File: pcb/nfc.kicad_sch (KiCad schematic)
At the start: 18 parts, among them U5 ST25R3916-AQWT, Y2 NX2016SA-27.12MHZ-STD-CZS-3

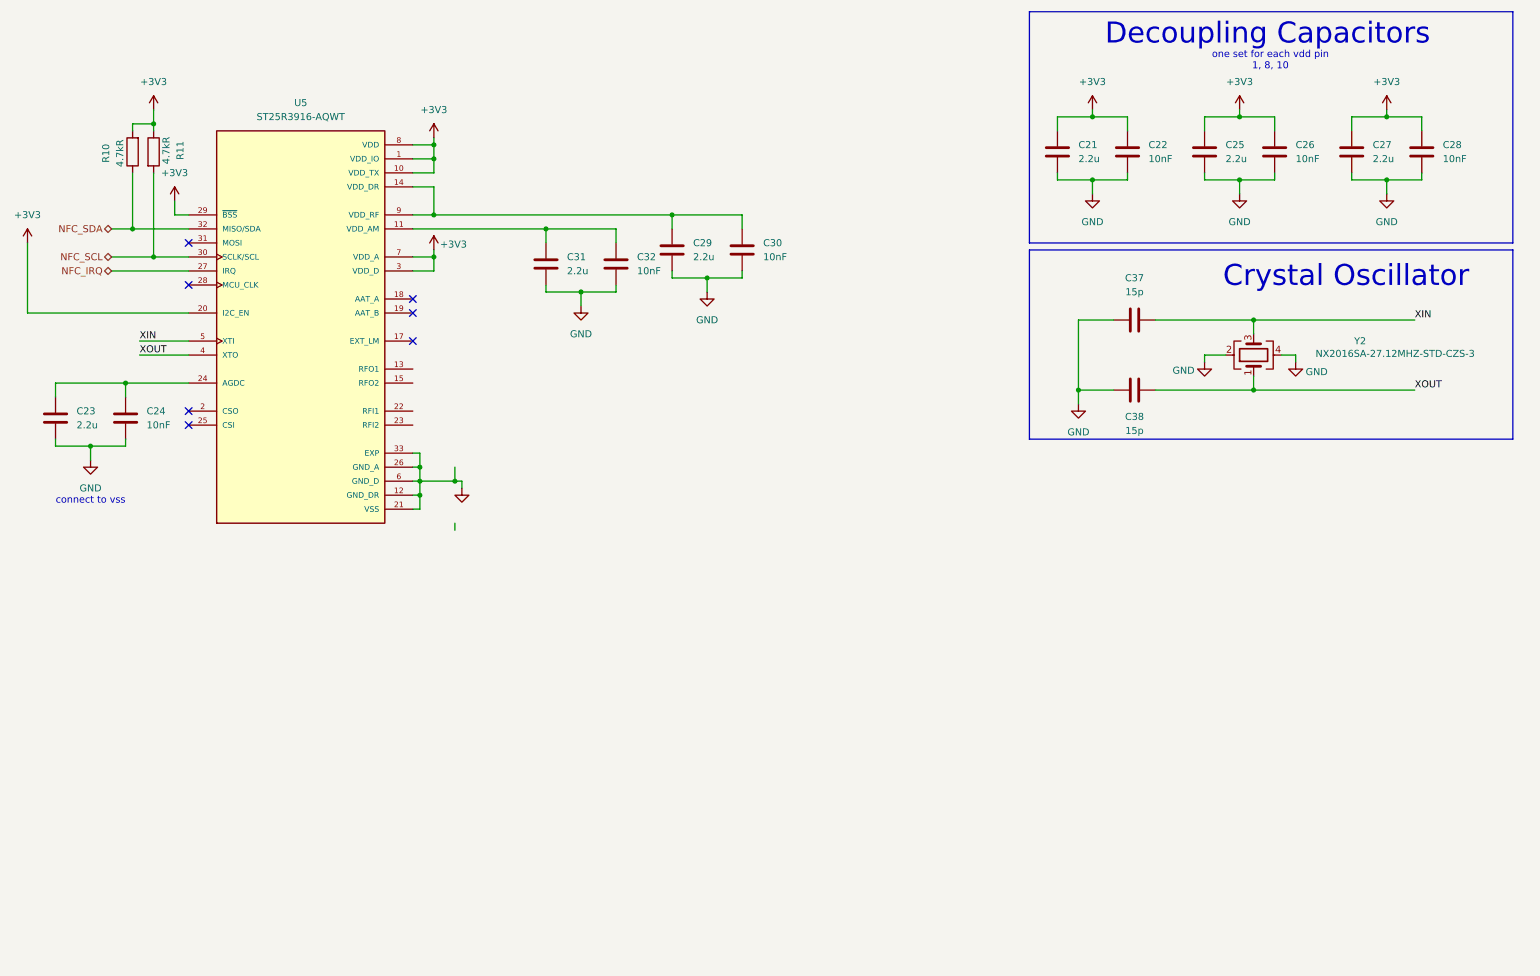
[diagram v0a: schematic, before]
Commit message: nfc tuning, new charger IC
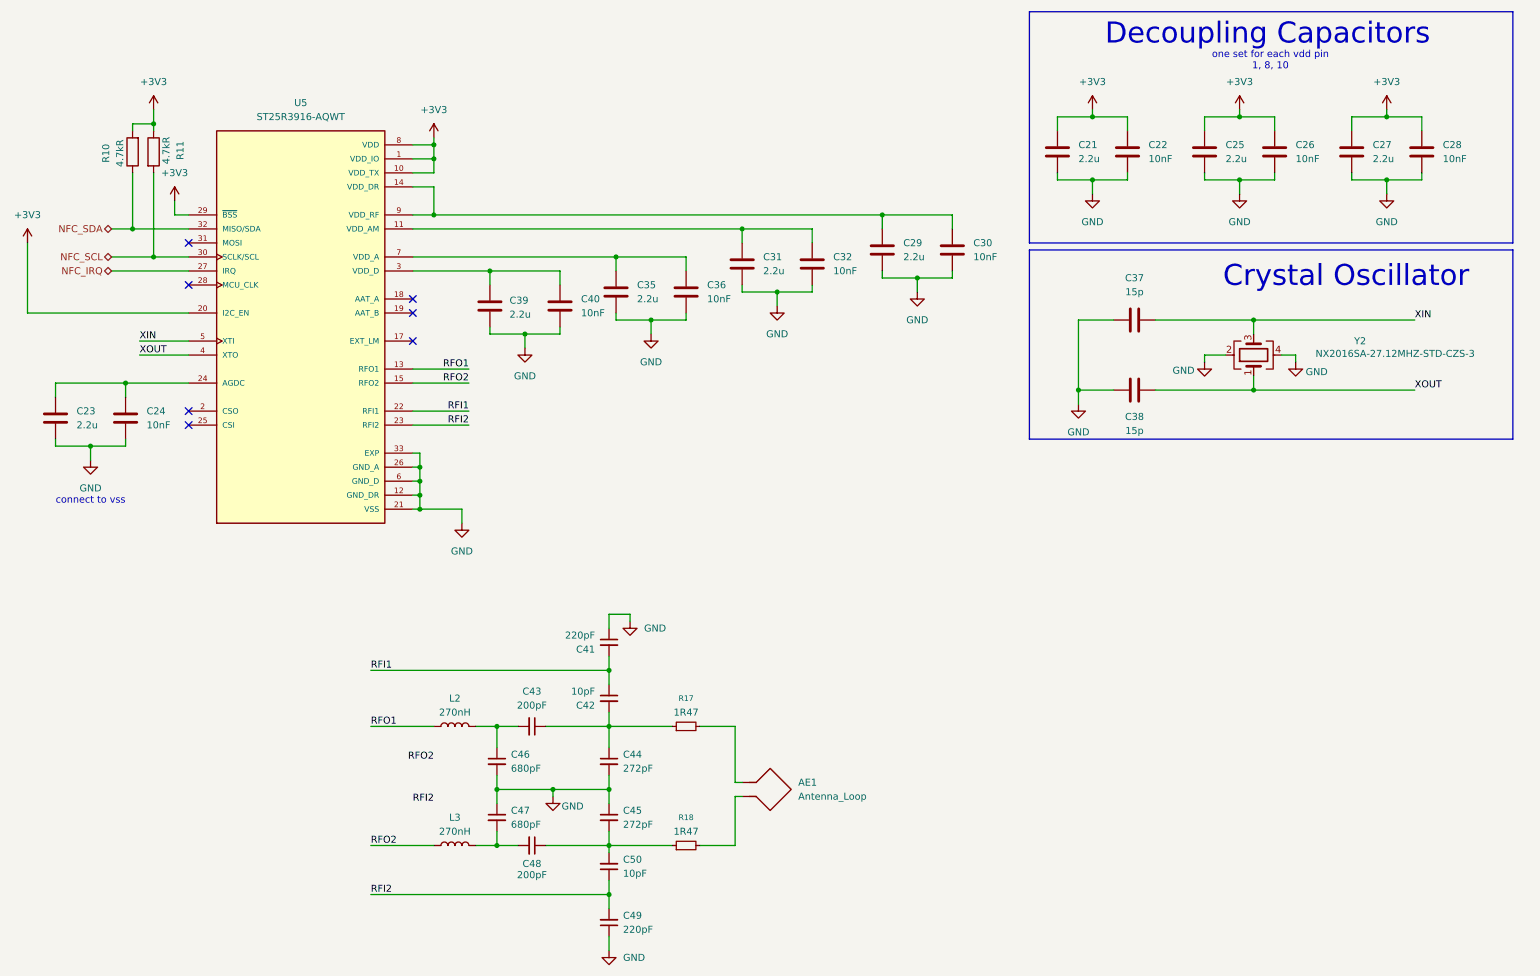
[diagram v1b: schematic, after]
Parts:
- added AE1: Antenna_Loop, pcb_coils:NFC, symbol Device:Antenna_Loop
- added C35, C39: 2.2u, symbol Device:C
- added C36, C40: 10nF, symbol Device:C
- added C41, C49: 220pF, symbol Device:C_Small
- added C42, C50: 10pF, symbol Device:C_Small
- added C43, C48: 200pF, symbol Device:C_Small
- added C44, C45: 272pF, symbol Device:C_Small
- added C46, C47: 680pF, symbol Device:C_Small
- added L2, L3: 270nH, symbol Device:L
- added R17, R18: 1R47, symbol Device:R_Small
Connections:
- net +3V3: no longer U5.3 (VDD_D), U5.7 (VDD_A)
- net GND: now also C35.2, C36.2, C39.2, C40.2, C41.1, C44.2, C45.1, C46.2, C47.1, C49.1
- net RFO1: now reaches U5.13 (RFO1)
- net RFO1: now also L2.1
- net RFO2: now reaches U5.15 (RFO2)
- net RFO2: now also L3.1
- net RFI1: now reaches U5.22 (RFI1)
- net RFI1: now also C41.2, C42.1
- net RFI2: now reaches U5.23 (RFI2)
- net RFI2: now also C49.2, C50.1
- new net: C35.1, C36.1, U5.7 (VDD_A)
- new net: C42.2, C43.1, C44.1, R17.1
- new net: C43.2, C46.1, L2.2
- new net: C47.2, C48.2, L3.2
- new net: AE1.1, R17.2
- new net: AE1.2, R18.2
- new net: C45.2, C48.1, C50.2, R18.1
- new net: C39.1, C40.1, U5.3 (VDD_D)
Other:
- moved on the sheet: C29, C30, C31, C32
